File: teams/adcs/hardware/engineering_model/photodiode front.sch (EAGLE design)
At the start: 15 parts, among them U1 LTC2483IDD

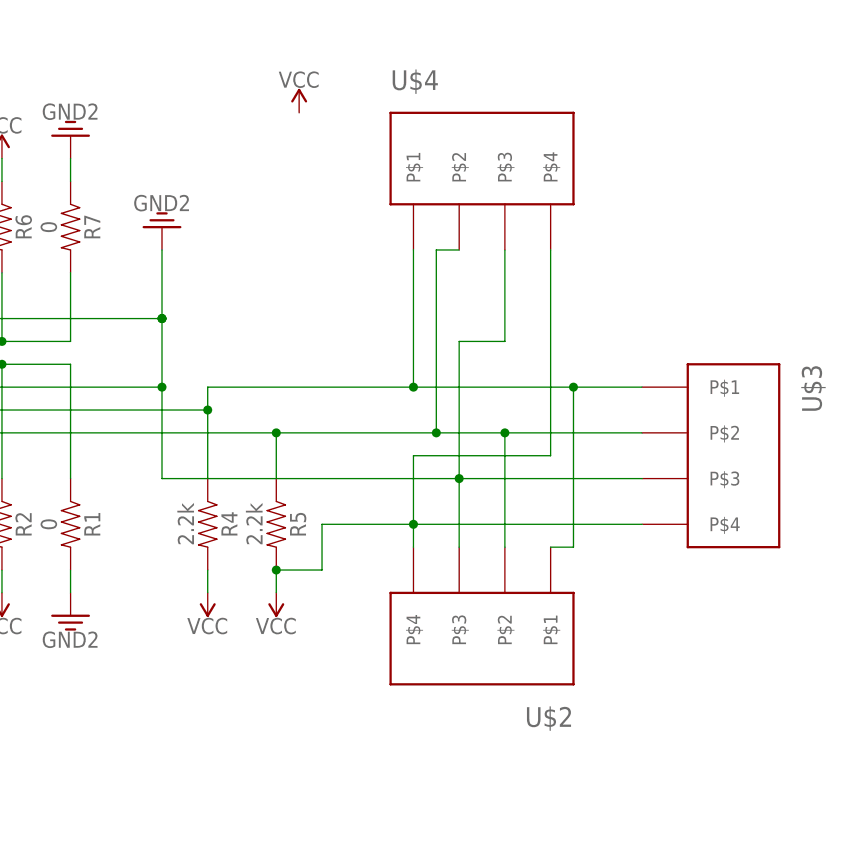
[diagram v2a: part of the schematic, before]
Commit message: ADCS/Photodiodes: A few aesthetic tweaks
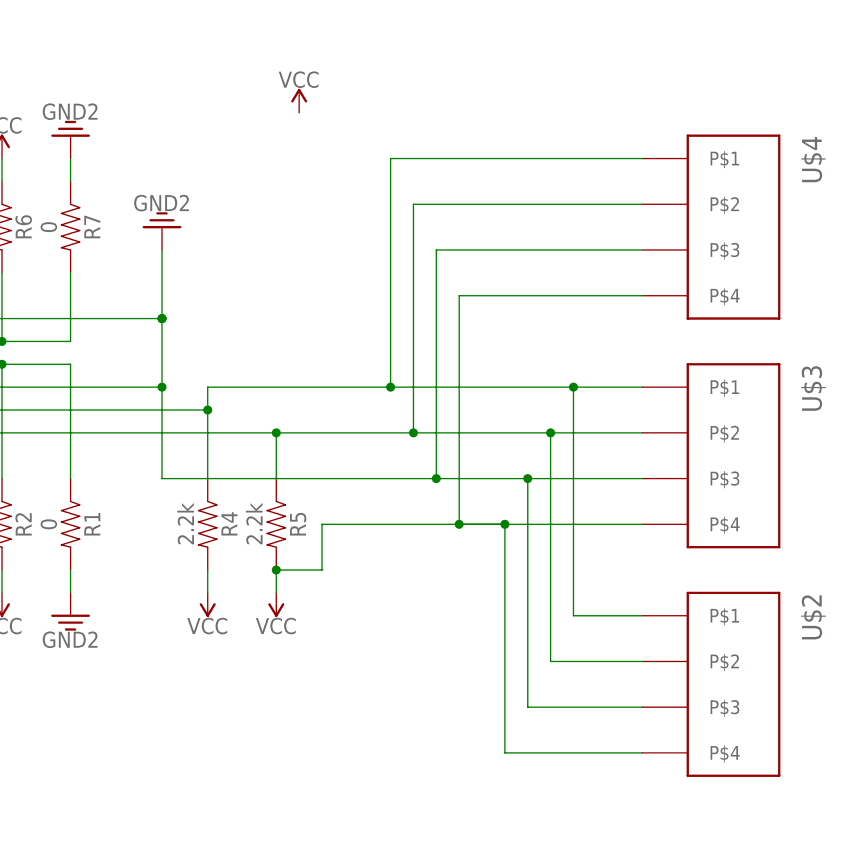
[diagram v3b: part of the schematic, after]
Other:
- moved on the sheet: U$2, U$4
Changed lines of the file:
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@@
 <instance part="GND" gate="G$1" x="129.54" y="78.74" rot="R180"/>
 <instance part="C2" gate="G$1" x="33.02" y="76.2"/>
-<instance part="U$2" gate="G$1" x="160.02" y="38.1" rot="R180"/>
-<instance part="U$4" gate="G$1" x="170.18" y="81.28"/>
+<instance part="U$2" gate="G$1" x="187.96" y="22.86" rot="R270"/>
+<instance part="U$4" gate="G$1" x="187.96" y="73.66" rot="R270"/>
 <instance part="SUPPLY9" gate="G$1" x="144.78" y="91.44"/>
 <instance part="U$3" gate="G$1" x="187.96" y="48.26" rot="R270"/>
@@
 <wire x1="142.24" y1="40.64" x2="142.24" y2="38.1" width="0.1524" layer="91"/>
 <pinref part="U$3" gate="G$1" pin="P$4"/>
-<wire x1="157.48" y1="45.72" x2="147.32" y2="45.72" width="0.1524" layer="91"/>
+<wire x1="167.64" y1="45.72" x2="147.32" y2="45.72" width="0.1524" layer="91"/>
 <wire x1="147.32" y1="45.72" x2="147.32" y2="40.64" width="0.1524" layer="91"/>
 <wire x1="147.32" y1="40.64" x2="142.24" y2="40.64" width="0.1524" layer="91"/>
 <junction x="142.24" y="40.64"/>
 <pinref part="U$4" gate="G$1" pin="P$4"/>
-<wire x1="172.72" y1="76.2" x2="172.72" y2="53.34" width="0.1524" layer="91"/>
 <pinref part="U$2" gate="G$1" pin="P$4"/>
-<wire x1="172.72" y1="53.34" x2="157.48" y2="53.34" width="0.1524" layer="91"/>
-<wire x1="157.48" y1="53.34" x2="157.48" y2="45.72" width="0.1524" layer="91"/>
-<wire x1="157.48" y1="45.72" x2="157.48" y2="43.18" width="0.1524" layer="91"/>
-<wire x1="182.88" y1="45.72" x2="157.48" y2="45.72" width="0.1524" layer="91"/>
-<junction x="157.48" y="45.72"/>
+<wire x1="182.88" y1="45.72" x2="167.64" y2="45.72" width="0.1524" layer="91"/>
+<junction x="167.64" y="45.72"/>
+<wire x1="162.56" y1="45.72" x2="167.64" y2="45.72" width="0.1524" layer="91"/>
+<wire x1="162.56" y1="45.72" x2="162.56" y2="71.12" width="0.1524" layer="91"/>
+<junction x="162.56" y="45.72"/>
+<wire x1="162.56" y1="71.12" x2="182.88" y2="71.12" width="0.1524" layer="91"/>
+<wire x1="182.88" y1="20.32" x2="167.64" y2="20.32" width="0.1524" layer="91"/>
+<wire x1="167.64" y1="20.32" x2="167.64" y2="45.72" width="0.1524" layer="91"/>
 </segment>
 </net>
@@
 <wire x1="142.24" y1="50.8" x2="142.24" y2="55.88" width="0.1524" layer="91"/>
 <pinref part="U$3" gate="G$1" pin="P$2"/>
-<wire x1="182.88" y1="55.88" x2="167.64" y2="55.88" width="0.1524" layer="91"/>
+<wire x1="182.88" y1="55.88" x2="172.72" y2="55.88" width="0.1524" layer="91"/>
 <junction x="142.24" y="55.88"/>
 <pinref part="U$2" gate="G$1" pin="P$2"/>
-<wire x1="167.64" y1="55.88" x2="160.02" y2="55.88" width="0.1524" layer="91"/>
-<wire x1="160.02" y1="55.88" x2="142.24" y2="55.88" width="0.1524" layer="91"/>
-<wire x1="167.64" y1="43.18" x2="167.64" y2="55.88" width="0.1524" layer="91"/>
-<junction x="167.64" y="55.88"/>
+<wire x1="172.72" y1="55.88" x2="157.48" y2="55.88" width="0.1524" layer="91"/>
+<wire x1="157.48" y1="55.88" x2="142.24" y2="55.88" width="0.1524" layer="91"/>
 <pinref part="U$4" gate="G$1" pin="P$2"/>
-<wire x1="162.56" y1="76.2" x2="160.02" y2="76.2" width="0.1524" layer="91"/>
-<wire x1="160.02" y1="76.2" x2="160.02" y2="55.88" width="0.1524" layer="91"/>
-<junction x="160.02" y="55.88"/>
+<wire x1="157.48" y1="81.28" x2="157.48" y2="55.88" width="0.1524" layer="91"/>
+<junction x="157.48" y="55.88"/>
+<wire x1="157.48" y1="81.28" x2="182.88" y2="81.28" width="0.1524" layer="91"/>
+<wire x1="182.88" y1="30.48" x2="172.72" y2="30.48" width="0.1524" layer="91"/>
+<wire x1="172.72" y1="30.48" x2="172.72" y2="55.88" width="0.1524" layer="91"/>
+<junction x="172.72" y="55.88"/>
 </segment>
 </net>
@@
 <pinref part="U$3" gate="G$1" pin="P$1"/>
 <wire x1="182.88" y1="60.96" x2="175.26" y2="60.96" width="0.1524" layer="91"/>
-<wire x1="175.26" y1="60.96" x2="157.48" y2="60.96" width="0.1524" layer="91"/>
-<wire x1="157.48" y1="60.96" x2="134.62" y2="60.96" width="0.1524" layer="91"/>
+<wire x1="175.26" y1="60.96" x2="154.94" y2="60.96" width="0.1524" layer="91"/>
+<wire x1="154.94" y1="60.96" x2="134.62" y2="60.96" width="0.1524" layer="91"/>
 <wire x1="134.62" y1="60.96" x2="134.62" y2="58.42" width="0.1524" layer="91"/>
 <junction x="134.62" y="58.42"/>
 <pinref part="U$4" gate="G$1" pin="P$1"/>
-<wire x1="157.48" y1="76.2" x2="157.48" y2="60.96" width="0.1524" layer="91"/>
-<junction x="157.48" y="60.96"/>
+<junction x="154.94" y="60.96"/>
 <pinref part="U$2" gate="G$1" pin="P$1"/>
-<wire x1="172.72" y1="43.18" x2="175.26" y2="43.18" width="0.1524" layer="91"/>
-<wire x1="175.26" y1="43.18" x2="175.26" y2="60.96" width="0.1524" layer="91"/>
 <junction x="175.26" y="60.96"/>
+<wire x1="154.94" y1="60.96" x2="154.94" y2="86.36" width="0.1524" layer="91"/>
+<wire x1="154.94" y1="86.36" x2="182.88" y2="86.36" width="0.1524" layer="91"/>
+<wire x1="182.88" y1="35.56" x2="175.26" y2="35.56" width="0.1524" layer="91"/>
+<wire x1="175.26" y1="35.56" x2="175.26" y2="60.96" width="0.1524" layer="91"/>
 </segment>
 </net>
@@
 <junction x="129.54" y="68.58"/>
 <pinref part="U$3" gate="G$1" pin="P$3"/>
-<wire x1="162.56" y1="50.8" x2="129.54" y2="50.8" width="0.1524" layer="91"/>
+<wire x1="160.02" y1="50.8" x2="129.54" y2="50.8" width="0.1524" layer="91"/>
 <wire x1="129.54" y1="50.8" x2="129.54" y2="60.96" width="0.1524" layer="91"/>
 <junction x="129.54" y="60.96"/>
 <pinref part="U$2" gate="G$1" pin="P$3"/>
-<wire x1="162.56" y1="43.18" x2="162.56" y2="50.8" width="0.1524" layer="91"/>
 <pinref part="U$4" gate="G$1" pin="P$3"/>
-<wire x1="162.56" y1="50.8" x2="162.56" y2="66.04" width="0.1524" layer="91"/>
-<wire x1="162.56" y1="66.04" x2="167.64" y2="66.04" width="0.1524" layer="91"/>
-<wire x1="167.64" y1="66.04" x2="167.64" y2="76.2" width="0.1524" layer="91"/>
-<wire x1="182.88" y1="50.8" x2="162.56" y2="50.8" width="0.1524" layer="91"/>
-<junction x="162.56" y="50.8"/>
+<wire x1="160.02" y1="50.8" x2="160.02" y2="76.2" width="0.1524" layer="91"/>
+<wire x1="182.88" y1="50.8" x2="170.18" y2="50.8" width="0.1524" layer="91"/>
+<junction x="160.02" y="50.8"/>
+<wire x1="170.18" y1="50.8" x2="160.02" y2="50.8" width="0.1524" layer="91"/>
+<wire x1="160.02" y1="76.2" x2="182.88" y2="76.2" width="0.1524" layer="91"/>
+<wire x1="182.88" y1="25.4" x2="170.18" y2="25.4" width="0.1524" layer="91"/>
+<wire x1="170.18" y1="25.4" x2="170.18" y2="50.8" width="0.1524" layer="91"/>
+<junction x="170.18" y="50.8"/>
 </segment>
 <segment>
